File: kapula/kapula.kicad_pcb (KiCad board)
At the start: 4 copper layers, 50 x 59 mm, 154 parts, among them J1 Conn_02x10_Odd_Even, J12 U.FL, J13 U.FL, J3 Conn_02x10_Odd_Even, J4 Conn_ARM_JTAG_SWD_10, J5 U.FL, J9 U.FL, Q1 AO3401A, Q2 AO3401A, Q3 AO3400A, Q4 BSS84, Q5 AO3400A, Q6 AO3400A, T1 BW21S7511A01TF, T2 BW21S7511A01TF, T3 BW21S7511A01TF, T4 BW21S7511A01TF, U1 XC6206P332MR, U2 TP4054, U3 DW01+G, U5 EFR32FG14P233F256GM48-B, U6 XA213-G4J, X1 DSB221SDN, Y1 32768 Hz

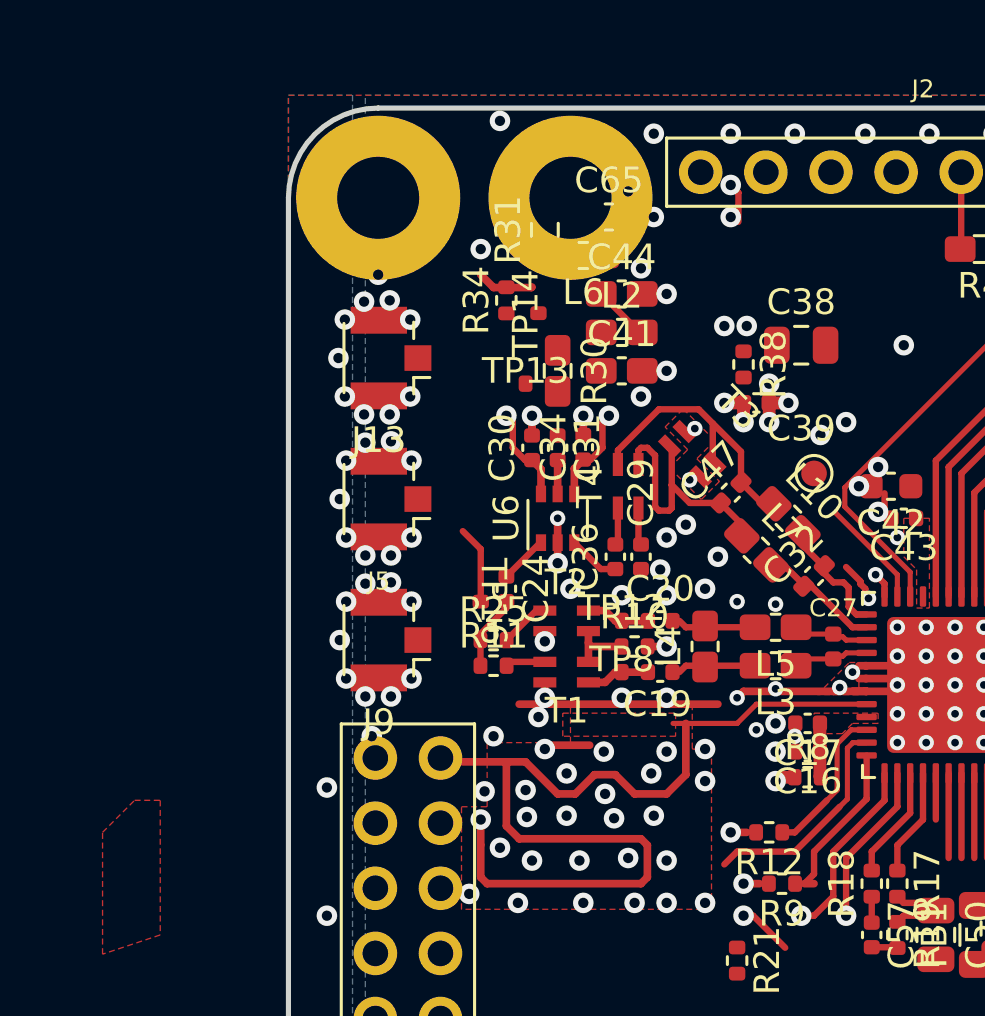
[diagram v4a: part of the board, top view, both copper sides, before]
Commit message: PCB: Organize lowpass components to fit them on board again
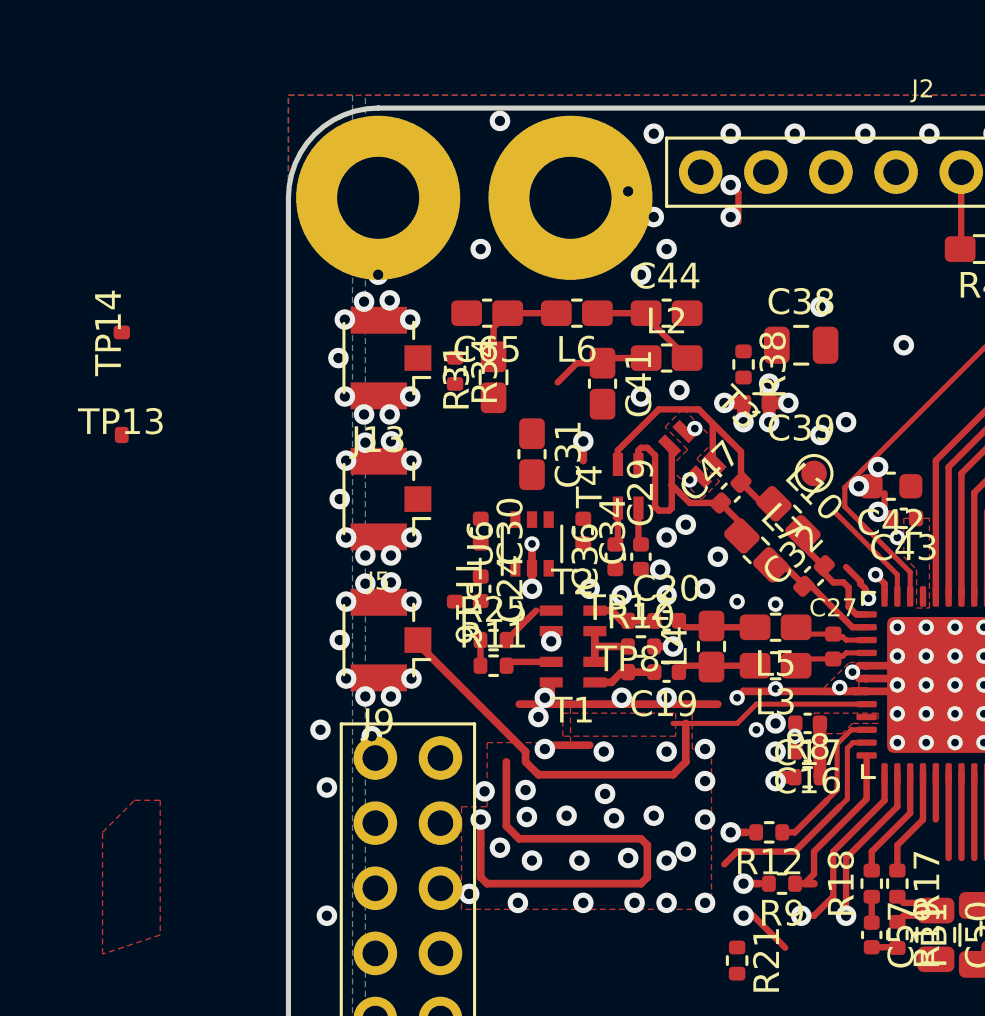
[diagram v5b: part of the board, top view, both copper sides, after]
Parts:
- removed R30: 0, kapula:R_0402_to_0603_HandSolder
- C31: footprint Capacitor_SMD:C_0402_1005Metric -> kapula:C_0402_to_0603_HandSolder
- moved TP14 16.3 mm to (93.5, 66.2)
- moved TP13 15.9 mm to (93.5, 70.2)
- moved R31 6.09 mm to (108.0, 68.0)
- moved C65 6.05 mm to (107.8, 65.5), turned to 180 degrees
- moved C30 3.82 mm to (107.5, 74.0), turned to -90 degrees
- moved R34 3.40 mm to (106.5, 67.8), turned to -90 degrees
- moved C34 3.27 mm to (111.5, 74.0), turned to -90 degrees
- moved L6 2.26 mm to (111.2, 65.5)
- moved L2 2.02 mm to (114.8, 67.2)
- moved C44 1.90 mm to (114.8, 65.5)
- moved U6 1.41 mm to (109.5, 74.5)
- moved C31 1.03 mm to (109.5, 71.0)
- moved C24 1.00 mm to (107.5, 76.2)
- moved TP16 1.00 mm to (106.5, 76.8)
- moved C41 0.90 mm to (112.2, 68.2), turned to -90 degrees
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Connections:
- C31 pad 1: /RF_TRX -> /FILT_TRX
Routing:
- net /FILT_TRX: track 0.00 -> 3.84 mm
- net /FILT_ANT: track 0.00 -> 3.83 mm
- net /TX_EN_SW: track 5.40 -> 1.62 mm, vias 2 -> 1
- net /RX_EN_SW: track 4.39 -> 0.62 mm, vias 2 -> 1
- net /RFP_RX: track 3.04 -> 0.00 mm
- net /RF_2G4: track 37.3 -> 39.8 mm
- net /ANT_UFL: track 2.22 -> 0.00 mm
- net Net-(C44-Pad1): track 2.22 -> 4.31 mm
- net /RFSW_TX: track 2.03 -> 0.04 mm
- net /RFSW_RX: track 1.90 -> 0.00 mm
- net /RF_RX: track 2.68 -> 1.00 mm
- net /RFSW_TRX: track 1.32 -> 0.00 mm
- net GND: track 93.2 -> 92.5 mm, vias 198 -> 197
- net /PAVDD: vias 3 -> 2

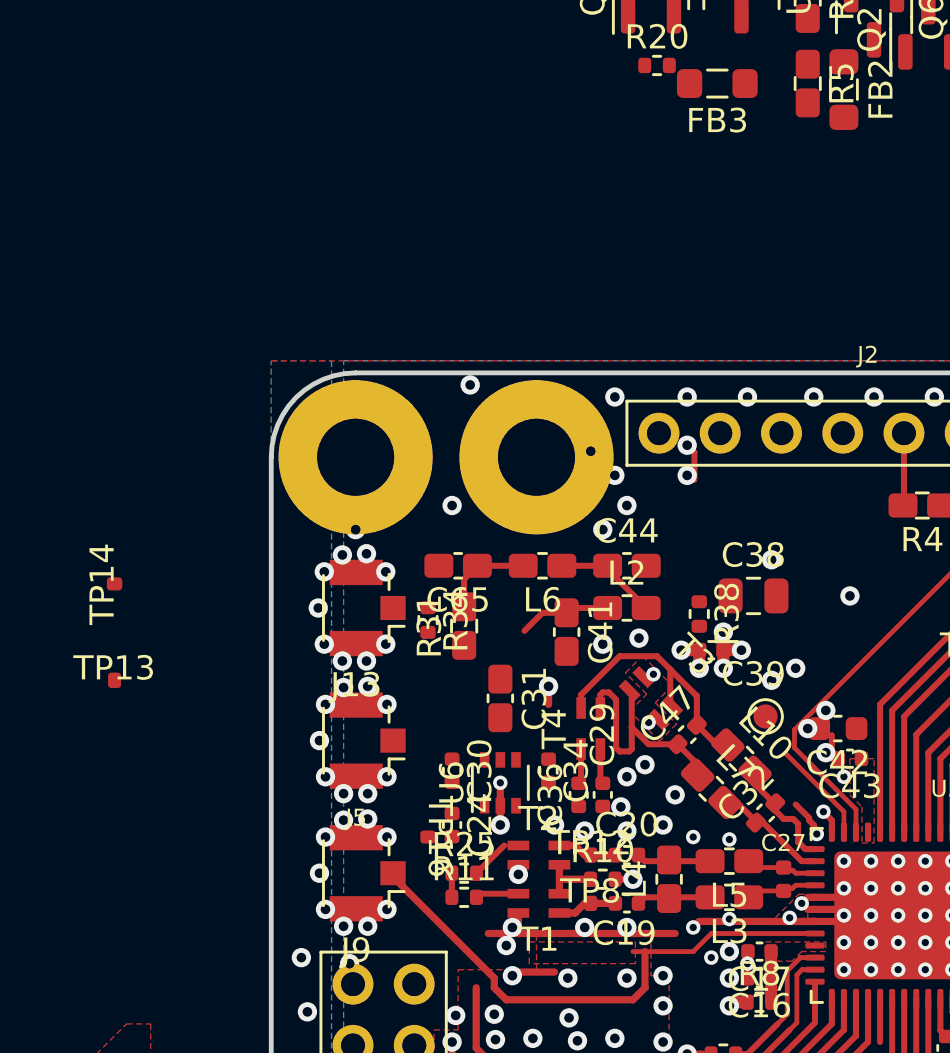
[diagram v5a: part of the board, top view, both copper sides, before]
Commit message: PCB: Squeeze TX balun in smaller area
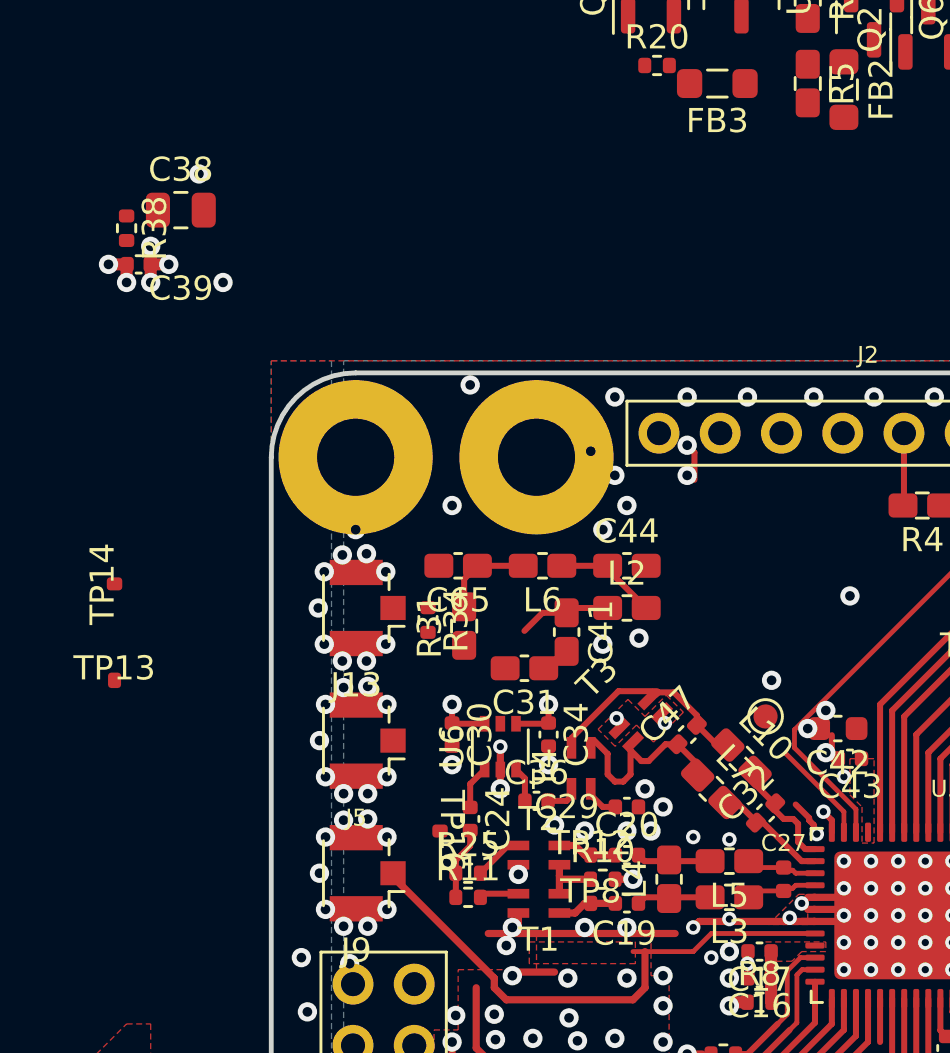
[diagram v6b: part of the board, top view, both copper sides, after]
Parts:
- moved C38 28.6 mm to (96.2, 50.8)
- moved C39 28.6 mm to (94.5, 53.0)
- moved R38 28.6 mm to (94.0, 51.5)
- moved C36 1.77 mm to (111.0, 75.2), turned to 0 degrees
- moved T4 1.70 mm to (112.8, 73.9)
- moved C31 1.60 mm to (110.5, 69.8), turned to 180 degrees
- moved C30 1.50 mm to (107.5, 72.5)
- moved C34 1.50 mm to (111.5, 72.5)
- moved U6 1.50 mm to (109.5, 73.0)
- moved C29 1.12 mm to (114.8, 75.5), turned to 180 degrees
- moved T3 1.02 mm to (115.3, 71.9), turned to 45 degrees
- moved C24 0.79 mm to (108.2, 76.0)
- moved TP16 0.56 mm to (107.0, 76.5)
- moved R11 0.17 mm to (108.2, 79.2)
- moved R25 0.17 mm to (108.2, 78.2)
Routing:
- net Net-(C47-Pad1): track 10.7 -> 7.92 mm
- net Net-(C47-Pad2): track 11.4 -> 8.92 mm
- net /TX_EN_SW: track 1.62 -> 3.76 mm, vias 1 -> 2
- net /RX_EN_SW: track 0.62 -> 2.76 mm, vias 1 -> 2
- net /RF_RX: track 1.00 -> 3.02 mm
- net /RFSW_RX: track 0.00 -> 1.82 mm
- net /RFSW_TX: track 0.04 -> 1.45 mm
- net GND: track 92.5 -> 91.7 mm, vias 197 -> 196

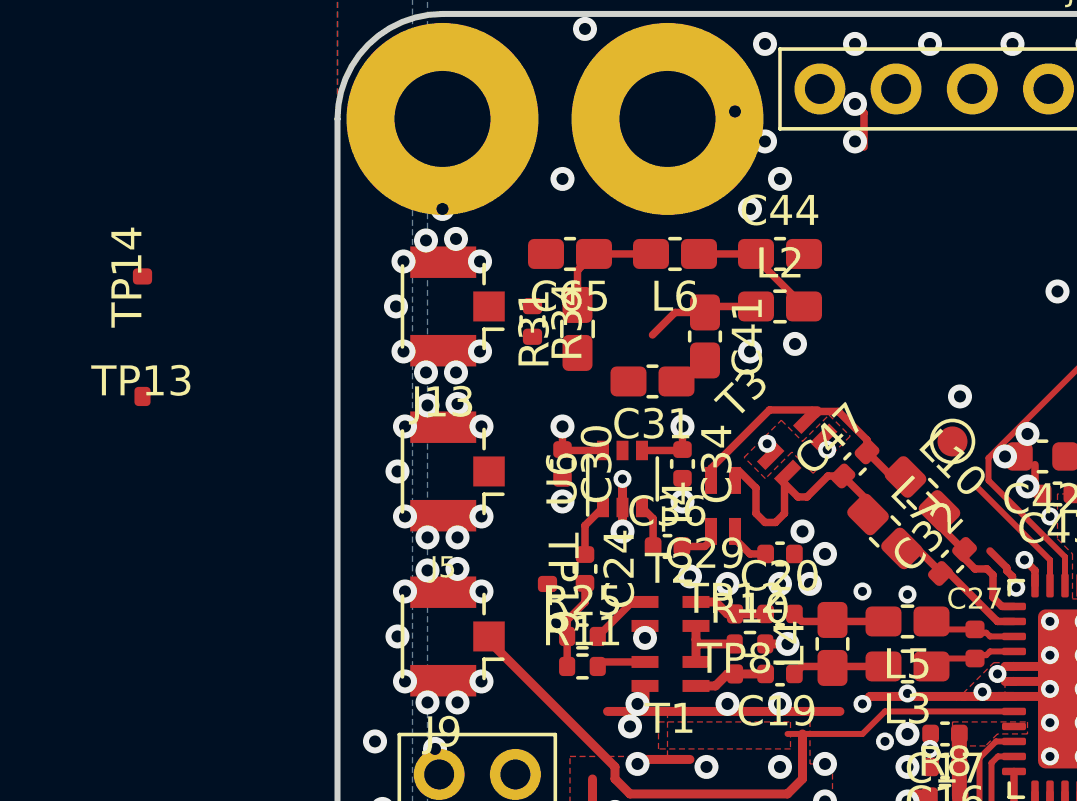
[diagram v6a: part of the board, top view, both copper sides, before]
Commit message: PCB: Route TX lowpass again
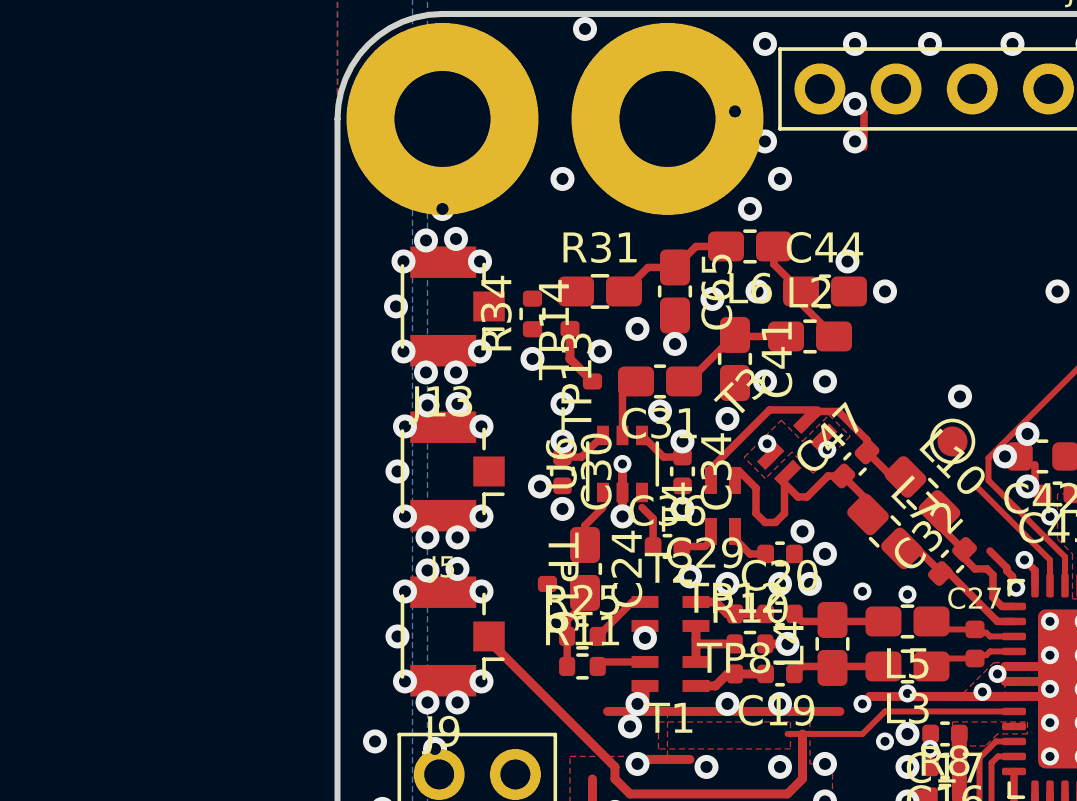
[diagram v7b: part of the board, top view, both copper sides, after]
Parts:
- C24: footprint Capacitor_SMD:C_0402_1005Metric -> kapula:C_0402_to_0603_HandSolder
- moved TP13 15.0 mm to (108.5, 69.8), turned to 90 degrees
- moved TP14 14.4 mm to (107.8, 68.0)
- moved C65 3.72 mm to (111.2, 66.8), turned to -90 degrees
- moved L6 2.51 mm to (113.8, 65.2)
- moved C44 1.95 mm to (116.2, 66.8)
- moved R31 1.46 mm to (108.8, 66.8), turned to 0 degrees
- moved L2 1.41 mm to (115.8, 68.2)
- moved C41 1.25 mm to (113.2, 69.0)
- moved U6 0.50 mm to (109.5, 72.5)
- moved C30 0.25 mm to (107.5, 72.8)
- moved C31 0.25 mm to (110.8, 69.8)
- moved C34 0.25 mm to (111.5, 72.8)
- moved R34 0.25 mm to (106.5, 67.5), turned to 90 degrees
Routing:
- net /FILT_BYPASS: track 0.00 -> 2.06 mm
- net /RFSW_TRX: track 0.00 -> 1.99 mm
- net GND: vias 196 -> 208

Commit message: PCB: Rearrange 2.4 GHz matching
TODO: check that its dimensions are correct
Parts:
- moved NT1 1.60 mm to (108.8, 86.8), turned to 180 degrees
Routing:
- net GND: track 91.7 -> 82.2 mm, vias 208 -> 230
